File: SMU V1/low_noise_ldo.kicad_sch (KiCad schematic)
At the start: 5 parts, among them U801 TPS7A2033PDBVR

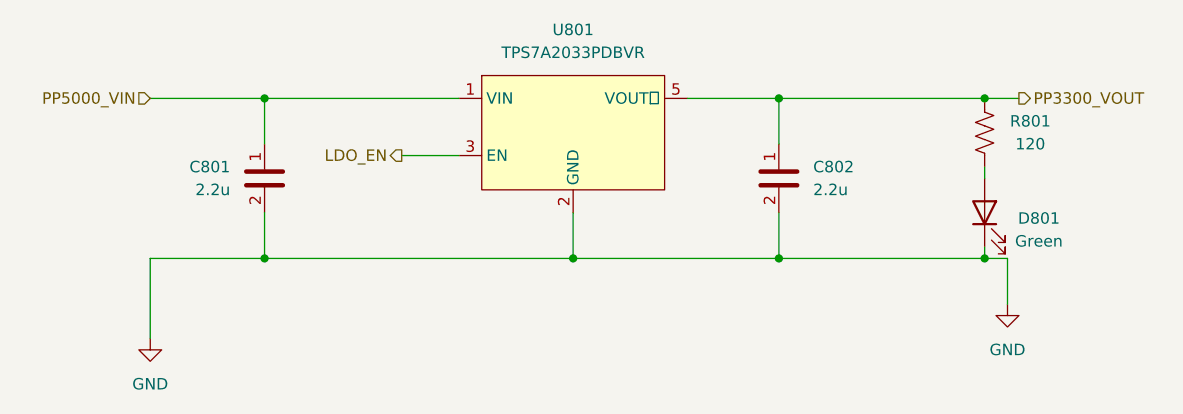
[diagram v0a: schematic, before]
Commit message: halfway done with routing, still needs antenna
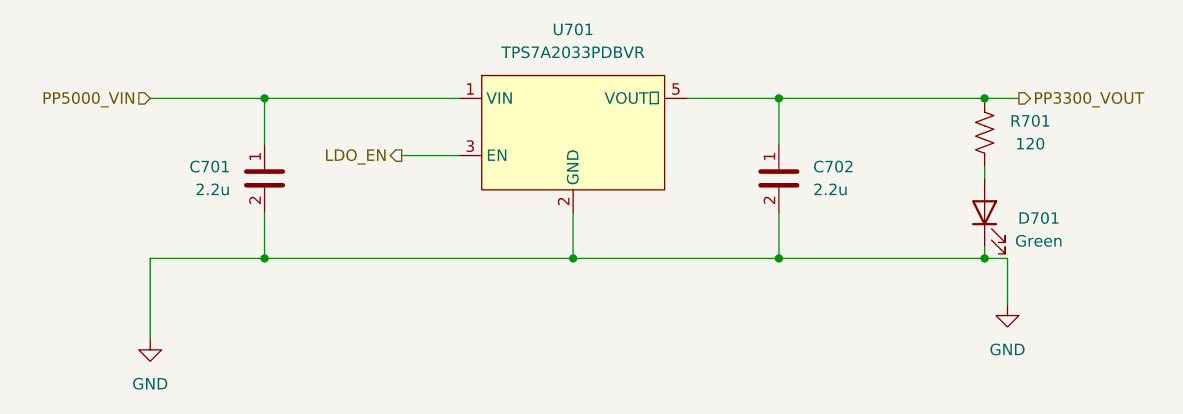
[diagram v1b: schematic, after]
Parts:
- renumbered C801 to C701, C802 to C702, D801 to D701, R801 to R701, U801 to U701
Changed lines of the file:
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@@
 		(dnp no)
 		(fields_autoplaced yes)
-		(property "Reference" "#PWR0802"
+		(property "Reference" "#PWR0702"
 			(at 196.85 115.57 0)
 			(effects
@@
 			(project "SMU V1"
 				(path "/1f58b889-96e6-4877-90a3-5a655db5910b/29d8e893-ab28-4f0b-b4ae-2fd3312ba121/209e2896-f8b9-4d4b-88ca-b4b8f94ef018"
+					(reference "#PWR0702")
+					(unit 1)
+				)
+				(path "/1f58b889-96e6-4877-90a3-5a655db5910b/4cd2b3ee-b9d4-4006-b5a4-98c8a3d3240f/b3165549-ffd4-4aee-a330-81bb01c2c5f2"
 					(reference "#PWR0802")
-					(unit 1)
-				)
-				(path "/1f58b889-96e6-4877-90a3-5a655db5910b/4cd2b3ee-b9d4-4006-b5a4-98c8a3d3240f/b3165549-ffd4-4aee-a330-81bb01c2c5f2"
-					(reference "#PWR0902")
 					(unit 1)
 				)
@@
 		(on_board yes)
 		(dnp no)
-		(property "Reference" "D801"
+		(property "Reference" "D701"
 			(at 200.3425 99.695 90)
 			(effects
@@
 			(project "SMU V1"
 				(path "/1f58b889-96e6-4877-90a3-5a655db5910b/29d8e893-ab28-4f0b-b4ae-2fd3312ba121/209e2896-f8b9-4d4b-88ca-b4b8f94ef018"
+					(reference "D701")
+					(unit 1)
+				)
+				(path "/1f58b889-96e6-4877-90a3-5a655db5910b/4cd2b3ee-b9d4-4006-b5a4-98c8a3d3240f/b3165549-ffd4-4aee-a330-81bb01c2c5f2"
 					(reference "D801")
-					(unit 1)
-				)
-				(path "/1f58b889-96e6-4877-90a3-5a655db5910b/4cd2b3ee-b9d4-4006-b5a4-98c8a3d3240f/b3165549-ffd4-4aee-a330-81bb01c2c5f2"
-					(reference "D901")
 					(unit 1)
 				)
@@
 		(dnp no)
 		(fields_autoplaced yes)
-		(property "Reference" "C802"
+		(property "Reference" "C702"
 			(at 175.26 93.9799 0)
 			(effects
@@
 			(project "SMU V1"
 				(path "/1f58b889-96e6-4877-90a3-5a655db5910b/29d8e893-ab28-4f0b-b4ae-2fd3312ba121/209e2896-f8b9-4d4b-88ca-b4b8f94ef018"
+					(reference "C702")
+					(unit 1)
+				)
+				(path "/1f58b889-96e6-4877-90a3-5a655db5910b/4cd2b3ee-b9d4-4006-b5a4-98c8a3d3240f/b3165549-ffd4-4aee-a330-81bb01c2c5f2"
 					(reference "C802")
-					(unit 1)
-				)
-				(path "/1f58b889-96e6-4877-90a3-5a655db5910b/4cd2b3ee-b9d4-4006-b5a4-98c8a3d3240f/b3165549-ffd4-4aee-a330-81bb01c2c5f2"
-					(reference "C902")
 					(unit 1)
 				)
@@
 		(on_board yes)
 		(dnp no)
-		(property "Reference" "R801"
+		(property "Reference" "R701"
 			(at 199.39 88.9 90)
 			(effects
@@
 			(project "SMU V1"
 				(path "/1f58b889-96e6-4877-90a3-5a655db5910b/29d8e893-ab28-4f0b-b4ae-2fd3312ba121/209e2896-f8b9-4d4b-88ca-b4b8f94ef018"
+					(reference "R701")
+					(unit 1)
+				)
+				(path "/1f58b889-96e6-4877-90a3-5a655db5910b/4cd2b3ee-b9d4-4006-b5a4-98c8a3d3240f/b3165549-ffd4-4aee-a330-81bb01c2c5f2"
 					(reference "R801")
-					(unit 1)
-				)
-				(path "/1f58b889-96e6-4877-90a3-5a655db5910b/4cd2b3ee-b9d4-4006-b5a4-98c8a3d3240f/b3165549-ffd4-4aee-a330-81bb01c2c5f2"
-					(reference "R901")
 					(unit 1)
 				)
@@
 		(dnp no)
 		(fields_autoplaced yes)
-		(property "Reference" "U801"
+		(property "Reference" "U701"
 			(at 148.59 78.74 0)
 			(effects
@@
 			(project "SMU V1"
 				(path "/1f58b889-96e6-4877-90a3-5a655db5910b/29d8e893-ab28-4f0b-b4ae-2fd3312ba121/209e2896-f8b9-4d4b-88ca-b4b8f94ef018"
+					(reference "U701")
+					(unit 1)
+				)
+				(path "/1f58b889-96e6-4877-90a3-5a655db5910b/4cd2b3ee-b9d4-4006-b5a4-98c8a3d3240f/b3165549-ffd4-4aee-a330-81bb01c2c5f2"
 					(reference "U801")
-					(unit 1)
-				)
-				(path "/1f58b889-96e6-4877-90a3-5a655db5910b/4cd2b3ee-b9d4-4006-b5a4-98c8a3d3240f/b3165549-ffd4-4aee-a330-81bb01c2c5f2"
-					(reference "U901")
 					(unit 1)
 				)
@@
 		(on_board yes)
 		(dnp no)
-		(property "Reference" "C801"
+		(property "Reference" "C701"
 			(at 110.49 93.9799 0)
 			(effects
@@
 			(project "SMU V1"
 				(path "/1f58b889-96e6-4877-90a3-5a655db5910b/29d8e893-ab28-4f0b-b4ae-2fd3312ba121/209e2896-f8b9-4d4b-88ca-b4b8f94ef018"
+					(reference "C701")
+					(unit 1)
+				)
+				(path "/1f58b889-96e6-4877-90a3-5a655db5910b/4cd2b3ee-b9d4-4006-b5a4-98c8a3d3240f/b3165549-ffd4-4aee-a330-81bb01c2c5f2"
 					(reference "C801")
-					(unit 1)
-				)
-				(path "/1f58b889-96e6-4877-90a3-5a655db5910b/4cd2b3ee-b9d4-4006-b5a4-98c8a3d3240f/b3165549-ffd4-4aee-a330-81bb01c2c5f2"
-					(reference "C901")
 					(unit 1)
 				)
@@
 		(on_board yes)
 		(dnp no)
-		(property "Reference" "#PWR0801"
+		(property "Reference" "#PWR0701"
 			(at 101.6 119.38 0)
 			(effects
@@
 			(project "SMU V1"
 				(path "/1f58b889-96e6-4877-90a3-5a655db5910b/29d8e893-ab28-4f0b-b4ae-2fd3312ba121/209e2896-f8b9-4d4b-88ca-b4b8f94ef018"
+					(reference "#PWR0701")
+					(unit 1)
+				)
+				(path "/1f58b889-96e6-4877-90a3-5a655db5910b/4cd2b3ee-b9d4-4006-b5a4-98c8a3d3240f/b3165549-ffd4-4aee-a330-81bb01c2c5f2"
 					(reference "#PWR0801")
 					(unit 1)
 				)
-				(path "/1f58b889-96e6-4877-90a3-5a655db5910b/4cd2b3ee-b9d4-4006-b5a4-98c8a3d3240f/b3165549-ffd4-4aee-a330-81bb01c2c5f2"
-					(reference "#PWR0901")
-					(unit 1)
-				)

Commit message: finished, should prob double check the high frequency stuff
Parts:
- D701: value Green -> GPS Power
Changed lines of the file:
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@@
 			)
 		)
-		(property "Value" "Green"
-			(at 200.3425 102.235 90)
+		(property "Value" "GPS Power"
+			(at 203.2 101.6 90)
 			(effects
 				(font
